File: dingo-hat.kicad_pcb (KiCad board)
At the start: 2 copper layers, 65 x 56 mm, 84 parts, among them J1 LiPo-Power, J10 PJ-038AH, J11 Bypass-Power, J12 Chassis-Out, J13 i2c_display, J14 NEOPIXEL, J15 MPU-9250, J16 i2c_display_1, J2 Raspberry_Pi_2_3, J24 M2.5_Mount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

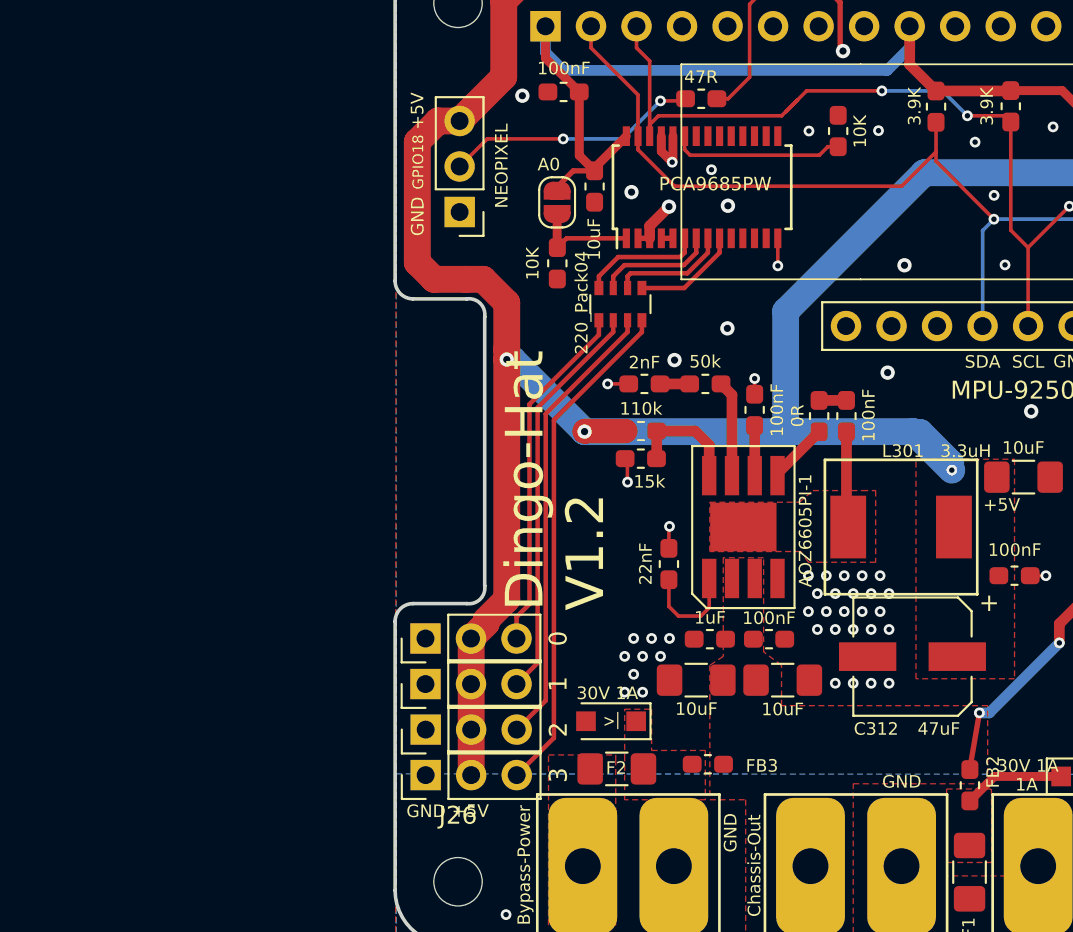
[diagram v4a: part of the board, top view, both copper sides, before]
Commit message: Flipping around the PWM header, making room for moving DC/DC.
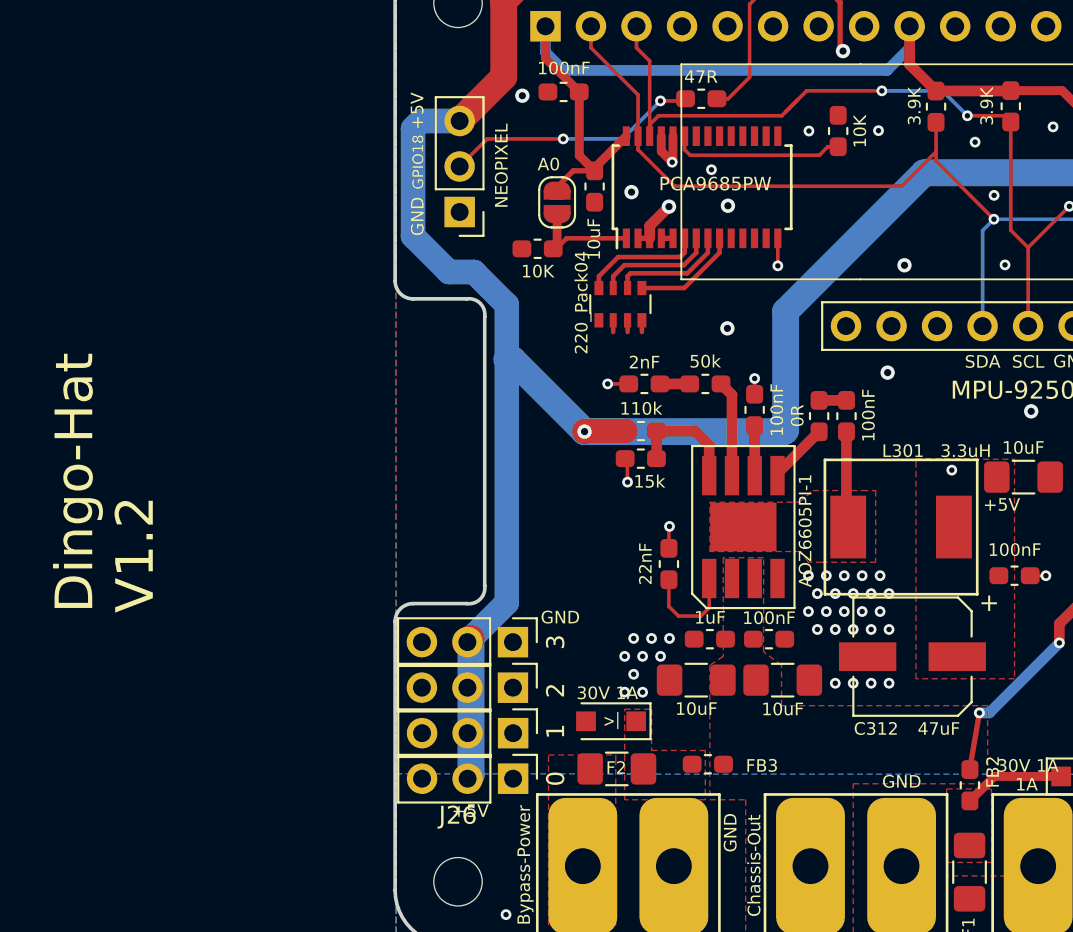
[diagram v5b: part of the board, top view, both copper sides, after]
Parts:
- moved J6 9.22 mm to (106.6, 90.3), turned to 270 degrees
- moved J9 8.88 mm to (106.6, 82.7), turned to 270 degrees
- moved J7 5.61 mm to (106.6, 87.7), turned to 270 degrees
- moved J8 5.40 mm to (106.6, 85.2), turned to 270 degrees
- moved R14 1.36 mm to (108.0, 60.7), turned to 180 degrees
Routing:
- net Net-(J9-Pad3): track 28.3 -> 0.65 mm
- net Net-(J8-Pad3): track 25.4 -> 0.65 mm
- net Net-(J7-Pad3): track 22.5 -> 0.65 mm
- net +5V: track 175.7 -> 155.1 mm, vias 4 -> 3
- net Net-(J6-Pad3): track 19.7 -> 0.00 mm
- net GND: vias 77 -> 76

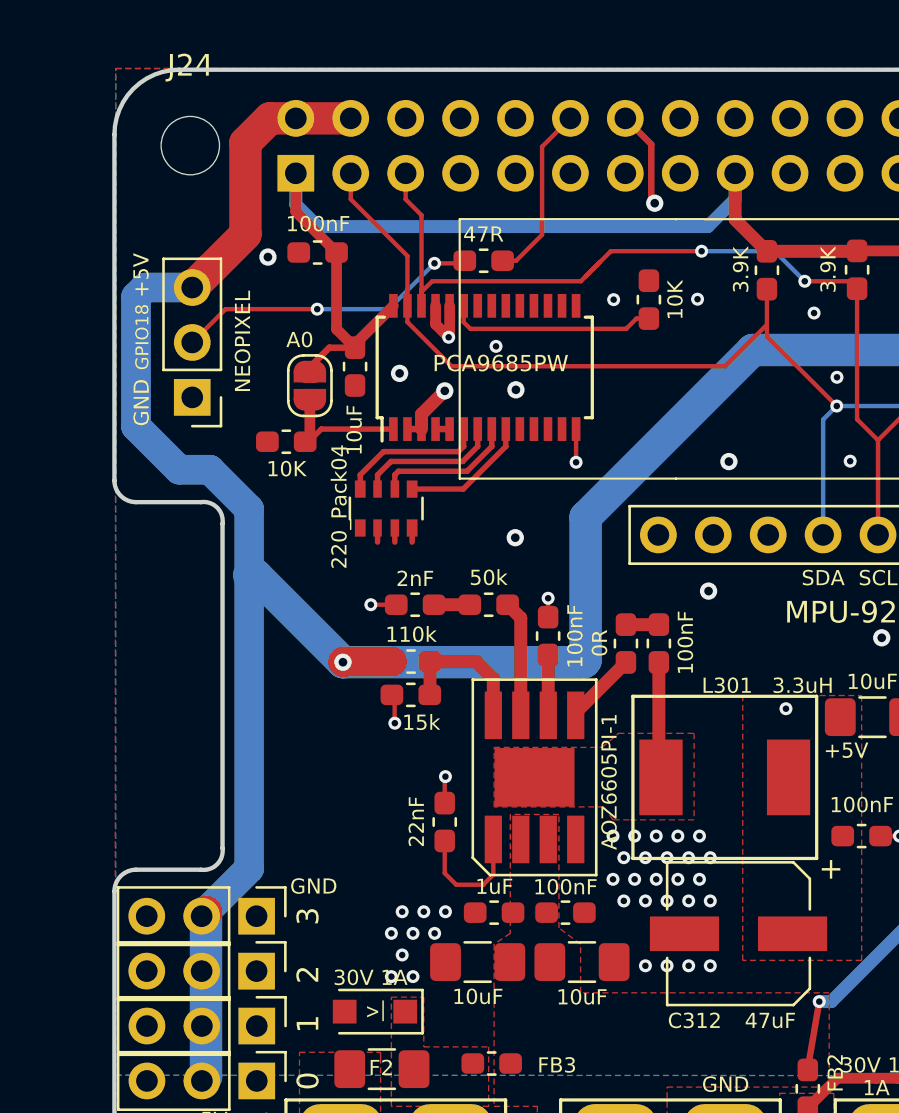
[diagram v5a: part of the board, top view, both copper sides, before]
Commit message: Ripping up, re-placing lots of stuff to make more room.
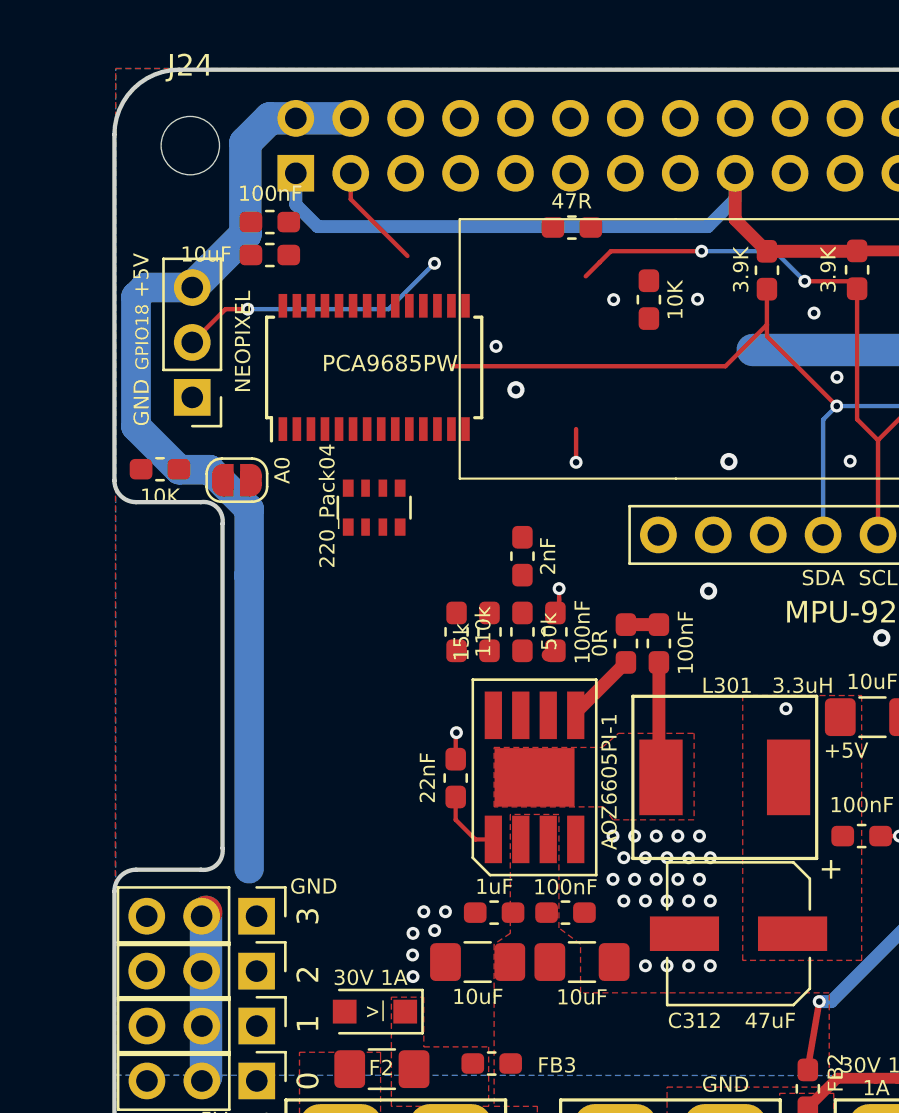
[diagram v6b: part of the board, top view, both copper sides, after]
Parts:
- moved C7 6.49 mm to (107.2, 52.1), turned to 180 degrees
- moved R14 5.98 mm to (102.1, 62.0)
- moved JP2 5.52 mm to (105.7, 62.5), turned to 180 degrees
- moved C310 5.45 mm to (118.9, 66.0), turned to 90 degrees
- moved U2 5.11 mm to (112.0, 57.3)
- moved R303 4.66 mm to (117.3, 69.5), turned to 270 degrees
- moved R2 4.36 mm to (121.2, 50.8)
- moved C8 2.62 mm to (107.2, 50.5)
- moved R304 2.51 mm to (115.8, 69.5), turned to 90 degrees
- moved C301 2.09 mm to (115.8, 76.3)
- moved R302 2.00 mm to (118.9, 69.5), turned to 270 degrees
- moved RN1 0.56 mm to (112.0, 63.8)
- moved C308 0.39 mm to (120.4, 69.5)
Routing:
- net +5V: track 155.1 -> 97.2 mm, vias 3 -> 2
- net /SCL_3.3: track 66.1 -> 50.3 mm
- net +3V3: track 78.3 -> 63.8 mm
- net GND: track 42.7 -> 30.0 mm, vias 76 -> 65
- net Net-(R7-Pad1): track 9.64 -> 0.00 mm
- net /GPIO18: track 8.25 -> 0.00 mm
- net Net-(R303-Pad2): track 8.04 -> 0.00 mm
- net /PWM0: track 6.79 -> 0.00 mm
- net /PWM1: track 6.64 -> 0.00 mm
- net /PWM2: track 6.49 -> 0.00 mm
- net /PWM3: track 5.95 -> 0.00 mm
- net /A0: track 5.95 -> 0.00 mm
- net /SDA_3.3: track 64.5 -> 58.6 mm
- net Net-(C308-Pad1): track 5.71 -> 0.01 mm
- net Net-(R302-Pad2): track 5.37 -> 0.00 mm
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
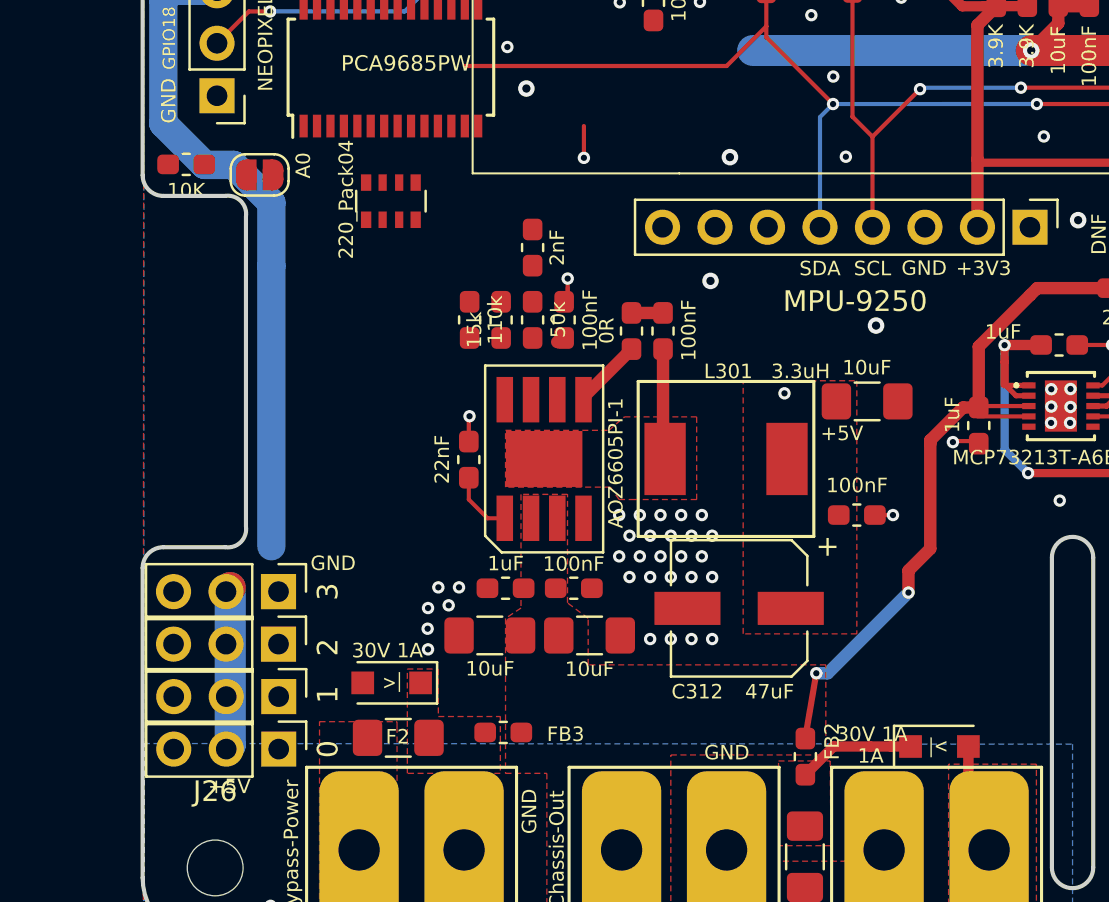
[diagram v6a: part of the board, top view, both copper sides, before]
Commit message: Smushing everything left to make room for that electrolytic as mentioned in #24
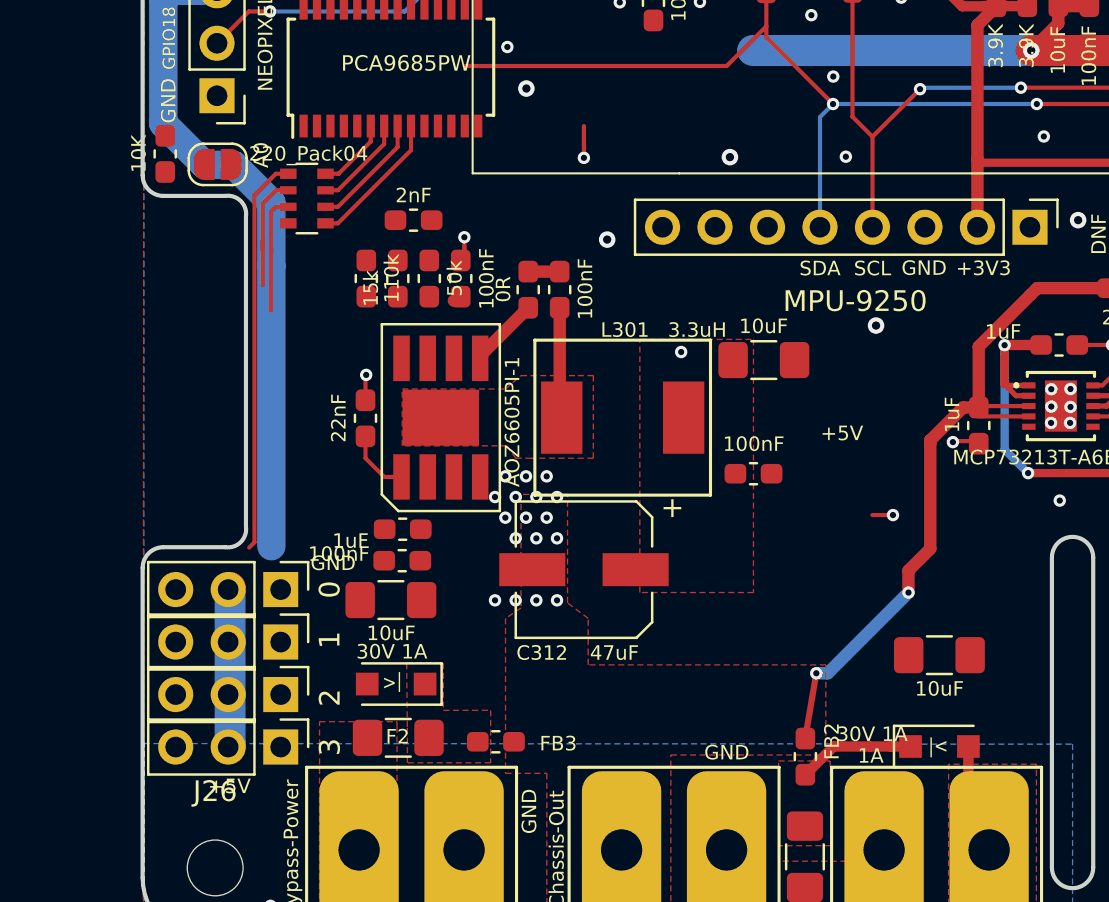
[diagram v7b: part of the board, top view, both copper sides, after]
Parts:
- moved C302 17.0 mm to (138.6, 85.7)
- moved C306 8.76 mm to (112.6, 79.6), turned to 180 degrees
- moved C312 7.74 mm to (121.4, 81.6)
- moved J6 7.72 mm to (106.7, 82.5)
- moved J9 7.52 mm to (106.7, 90.2)
- moved C310 5.91 mm to (113.1, 64.7), turned to 180 degrees
- moved C301 5.39 mm to (110.8, 74.3)
- moved C307 5.39 mm to (120.2, 68.0)
- moved C308 5.39 mm to (115.4, 67.5)
- moved C309 5.39 mm to (129.6, 76.9)
- moved C311 5.39 mm to (130.1, 71.4)
- moved R301 5.39 mm to (118.7, 68.0)
- moved R302 5.39 mm to (113.9, 67.5)
- moved R303 5.39 mm to (112.3, 67.5)
- moved R304 5.39 mm to (110.8, 67.5)
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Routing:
- net Net-(J6-Pad3): track 0.00 -> 19.2 mm
- net /PWM3: track 0.00 -> 6.77 mm
- net Net-(J7-Pad3): track 0.00 -> 5.96 mm
- net Net-(J8-Pad3): track 0.00 -> 5.93 mm
- net /PWM2: track 0.00 -> 5.70 mm
- net /PWM1: track 0.00 -> 4.63 mm
- net /PWM0: track 0.00 -> 3.58 mm
- net GND: vias 65 -> 52

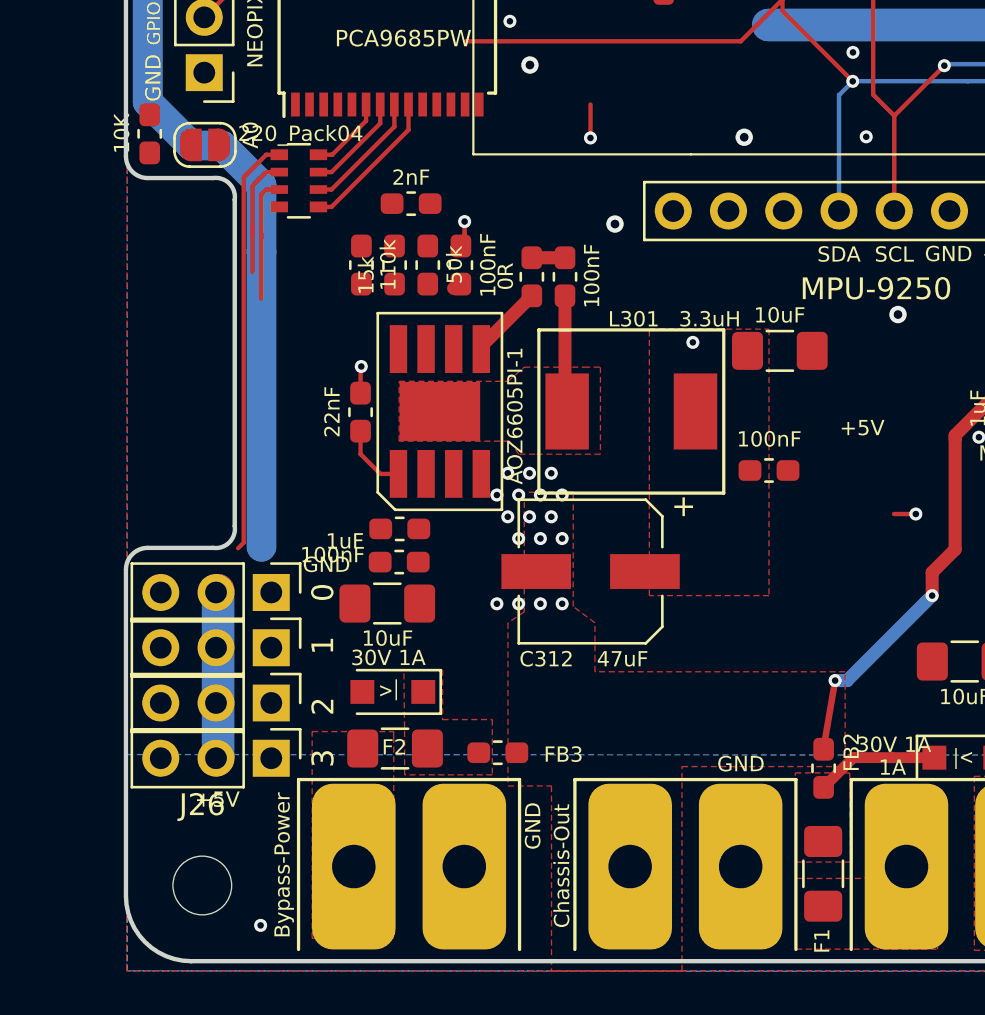
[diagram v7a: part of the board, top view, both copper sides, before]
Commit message: More compacting, improvement on space utilization. Closes #24.
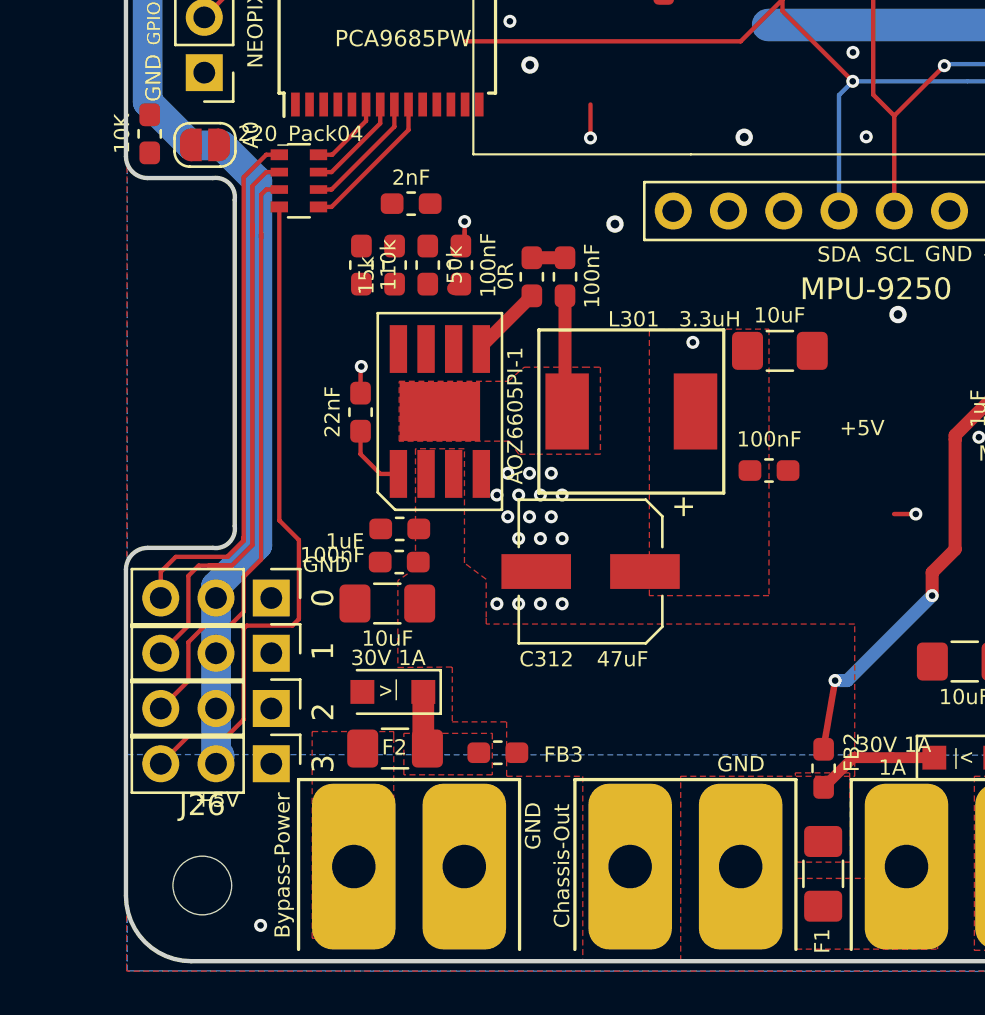
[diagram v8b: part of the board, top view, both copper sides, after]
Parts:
- moved G3 22.0 mm to (182.4, 81.5)
- moved J6 0.25 mm to (106.7, 82.8)
- moved J8 0.25 mm to (106.7, 87.9)
- moved J9 0.25 mm to (106.7, 90.4)
- moved J7 0.25 mm to (106.7, 85.3)
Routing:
- net Net-(J9-Pad3): track 0.00 -> 30.9 mm
- net Net-(J8-Pad3): track 5.93 -> 27.3 mm
- net Net-(J7-Pad3): track 5.96 -> 27.1 mm
- net Net-(J6-Pad3): track 19.2 -> 25.6 mm
- net +5V: track 97.2 -> 100.3 mm
- net Net-(D3-Pad1): track 0.00 -> 2.68 mm
